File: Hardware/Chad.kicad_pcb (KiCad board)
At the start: 4 copper layers, 30 x 60 mm, 119 parts, among them J1 RBUS, J2 GPIO Breakout, J3 ServoCH1, J4 ServoCH2, J5 USB_C_Receptacle_USB2.0, U1 ESP32-S3, U2 SN65HVD230, U3 LM66200DRLR, U4 MAX77827AEFD+T, U5 SC4215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

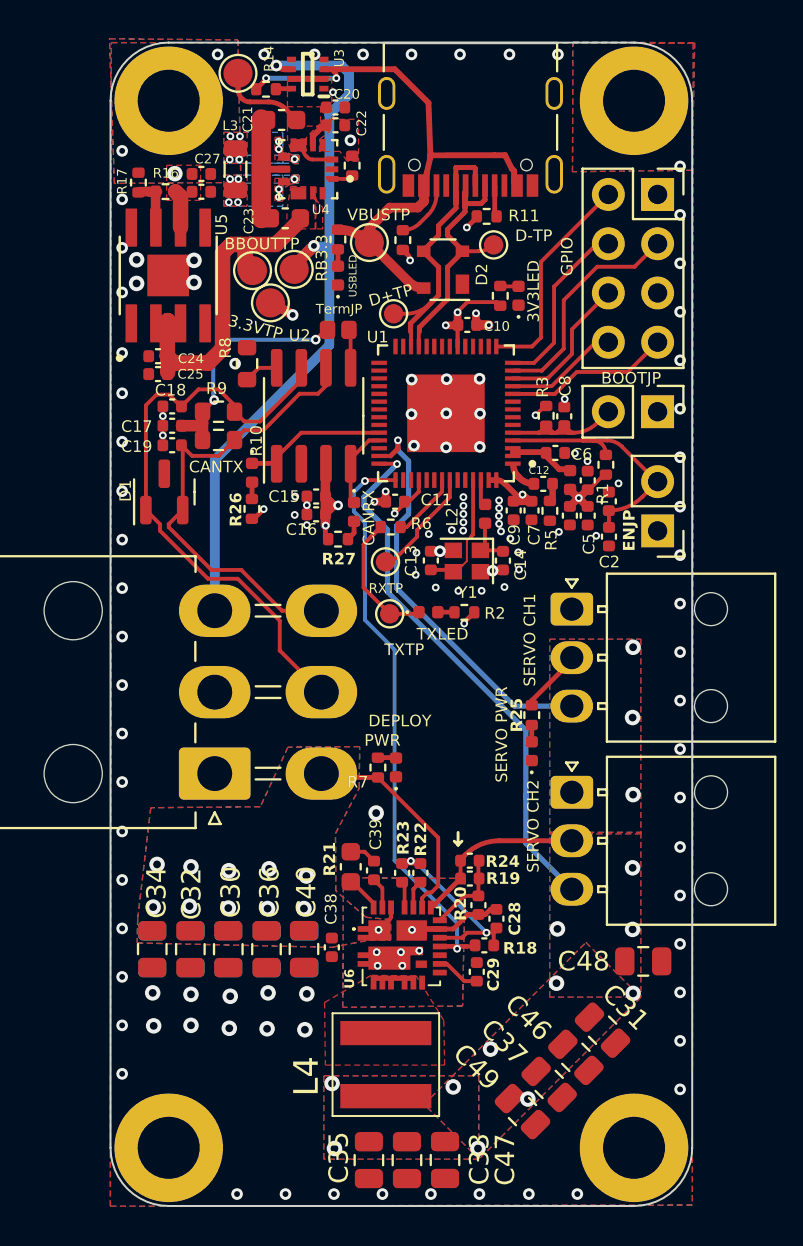
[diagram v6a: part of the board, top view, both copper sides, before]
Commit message: fixed via numbers, added gpio pullup option, need to decide PGood flag
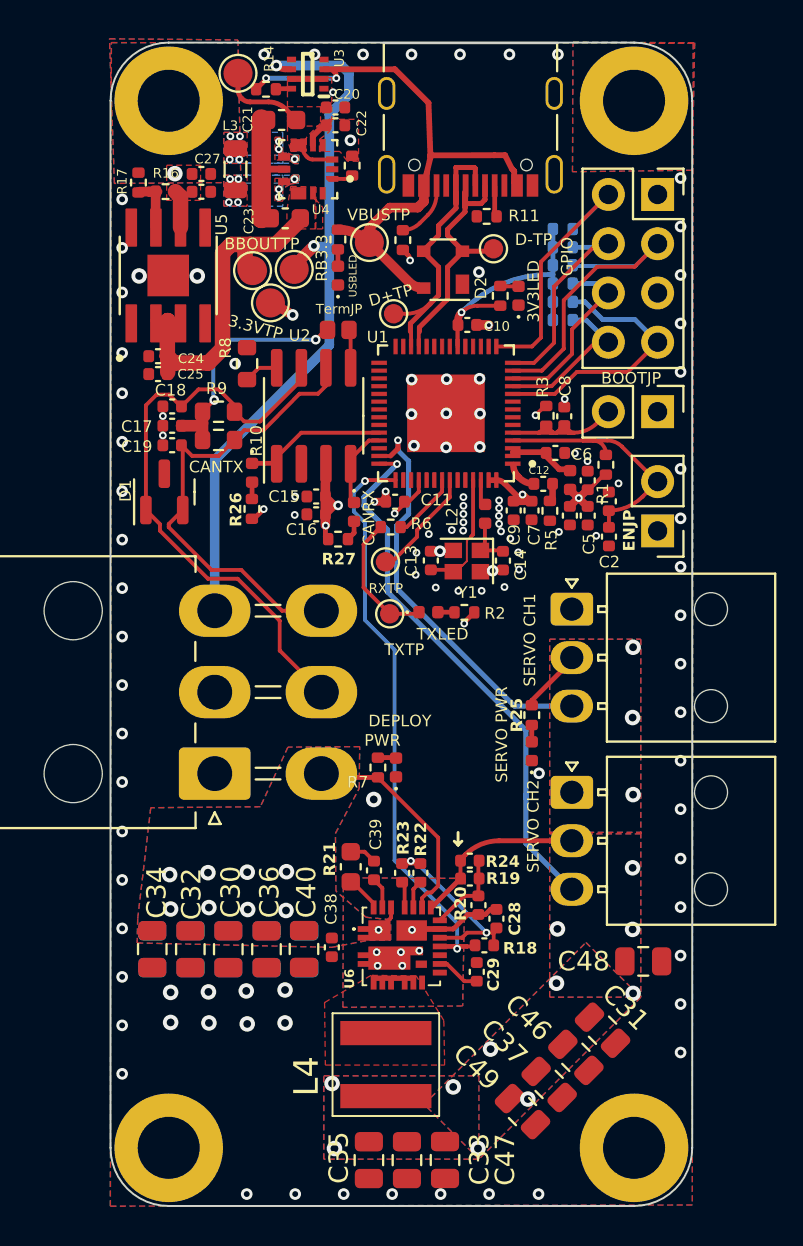
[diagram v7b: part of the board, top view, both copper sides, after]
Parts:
- added R28: DNP, Resistor_SMD:R_0402_1005Metric, B.Cu at (55.3, 52.6)
- added R29: DNP, Resistor_SMD:R_0402_1005Metric, B.Cu at (55.3, 53.6)
- added R30: DNP, Resistor_SMD:R_0402_1005Metric, B.Cu at (55.3, 54.5)
- added R31: DNP, Resistor_SMD:R_0402_1005Metric, B.Cu at (55.3, 51.7)
- added R32: DNP, Resistor_SMD:R_0402_1005Metric, B.Cu at (55.3, 55.5)
- added R33: DNP, Resistor_SMD:R_0402_1005Metric, B.Cu at (55.3, 56.4)
- R26, R27: value 470 -> 1k
- moved G*** 2.69 mm to (44.9, 60.0)
- moved TP1 0.20 mm to (51.8, 52.7)
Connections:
- C28 pad 1: GND -> GNDA
- C38 pad 2: GND -> GNDA
- R20 pad 1: GND -> GNDA
- R23 pad 2: /buckC/VDD -> GNDA
- U6 pad 16: GND -> GNDA
- U6 pad 25: GND -> GNDA
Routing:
- net +3V3: track 28.2 -> 37.1 mm, vias 12 -> 11
- net GND: track 15.4 -> 9.35 mm, vias 130 -> 118
- net /GPIO4: track 8.58 -> 13.8 mm
- net /GPIO1: track 11.6 -> 16.5 mm
- net GNDA: track 0.00 -> 4.83 mm, vias 0 -> 1
- net /GPIO0: track 11.3 -> 13.9 mm
- net /GPIO5: track 5.87 -> 8.19 mm
- net /GPIO3: track 7.50 -> 9.54 mm
- net /GPIO2: track 9.18 -> 11.1 mm
- net +12V: vias 11 -> 9

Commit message: v2 finished? (pre-review)
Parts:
- added R34: 2.2k, Resistor_SMD:R_0402_1005Metric, F.Cu at (46.5, 75.2)
- added R35: 1.5k, Resistor_SMD:R_0402_1005Metric, F.Cu at (47.4, 75.2)
- moved R27 0.10 mm to (43.6, 67.7)
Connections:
- C28 pad 1: GNDA -> GND
- C38 pad 2: GNDA -> GND
- R18 pad 2: /BuckPGOOD -> /buckC/PGOOD
- R20 pad 1: GNDA -> GND
- R23 pad 2: GNDA -> GND
- U6 pad 14: /BuckPGOOD -> /buckC/PGOOD
- U6 pad 16: GNDA -> GND
- U6 pad 25: GNDA -> GND
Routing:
- net /BuckPGOOD: track 31.5 -> 13.8 mm
- net /buckC/PGOOD: track 0.00 -> 17.2 mm, vias 0 -> 2
- net GND: track 9.35 -> 24.8 mm, vias 118 -> 116
- net GNDA: track 4.83 -> 0.00 mm, vias 1 -> 0
- net VBUS: track 31.6 -> 33.1 mm
- net /TXD: track 7.69 -> 6.68 mm
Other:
- board text removed: "C - CAN H - H-Bridge A - Actuator D - DC"
